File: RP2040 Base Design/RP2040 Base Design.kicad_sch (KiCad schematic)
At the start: 27 parts, among them J1 USB_B_Micro, J2 Conn_01x02, J3 RP2040_SWD, U1 RP2040, U2 AMS1117-3.3, U3 W25Q128JVS, Y1 X322512MSB4SI

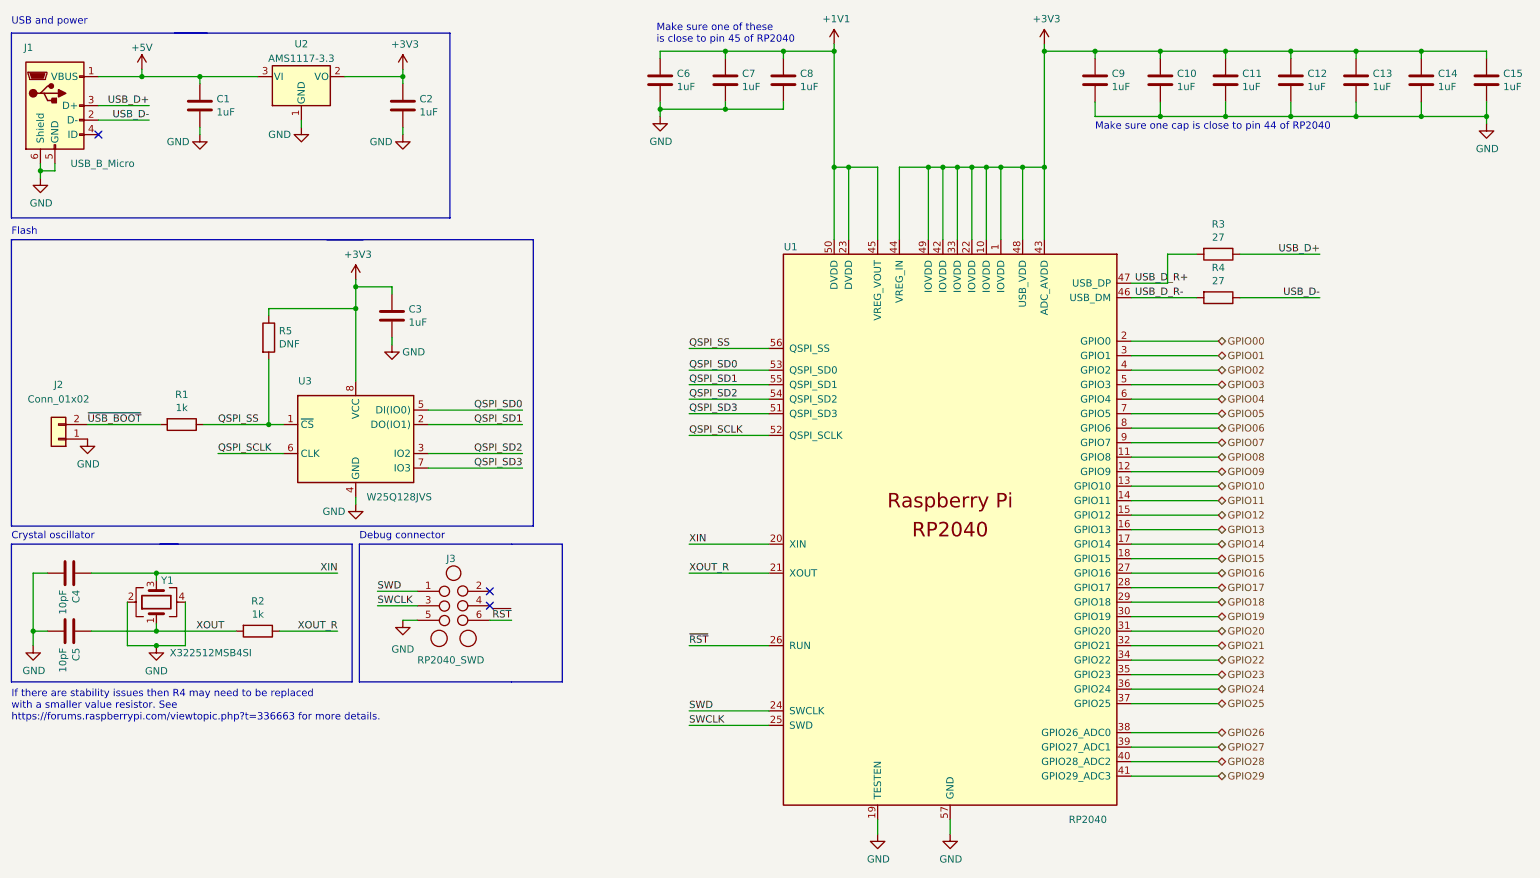
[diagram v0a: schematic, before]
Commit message: Move RP2040 to subsheet, fix up column names
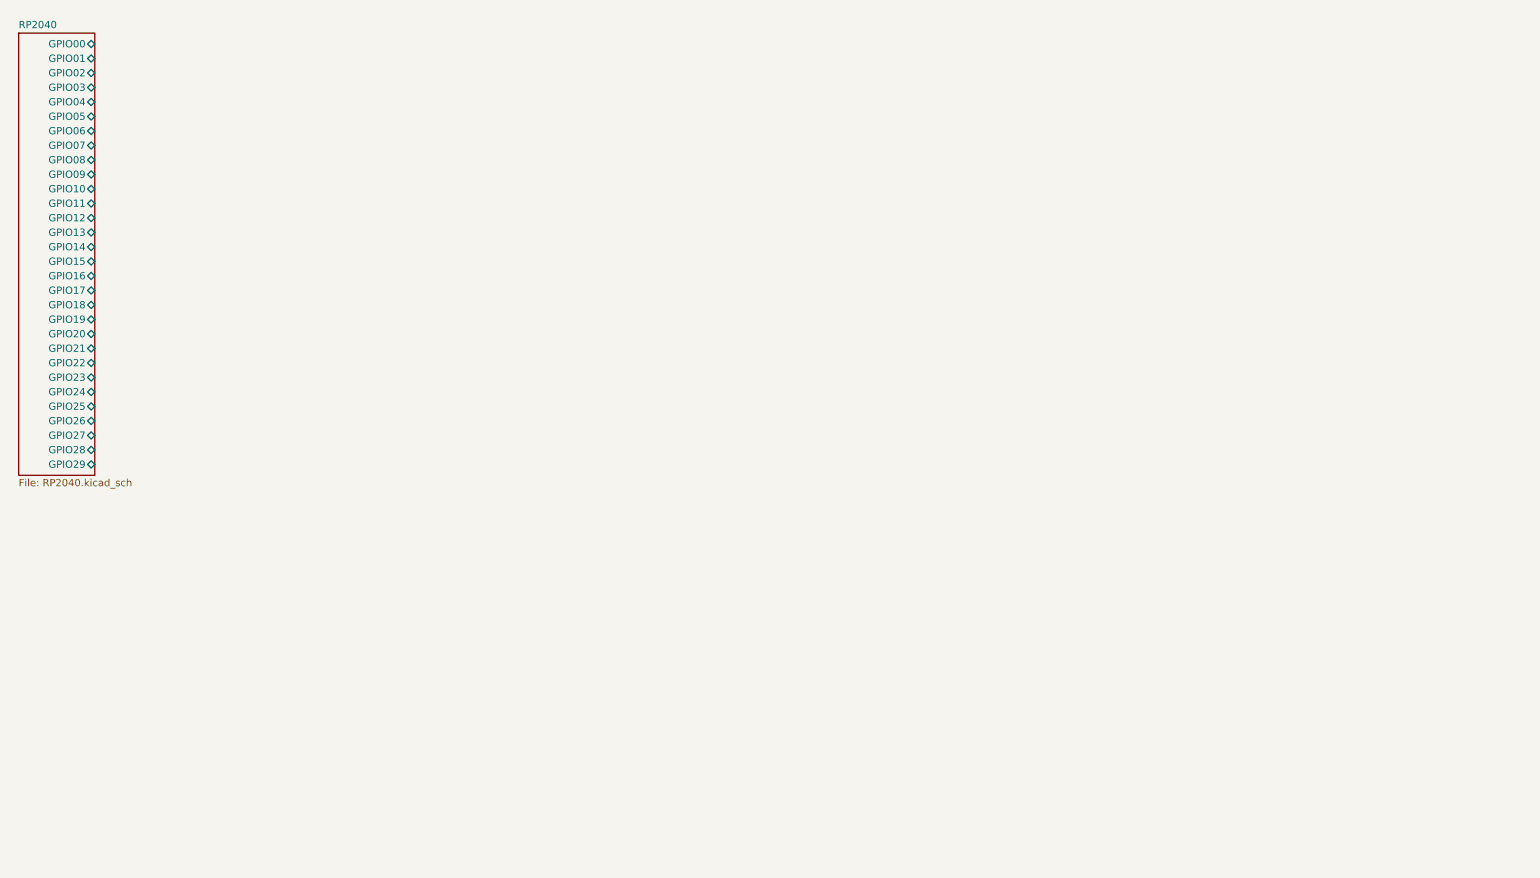
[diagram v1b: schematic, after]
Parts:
- removed C1, C10, C11, C12, C13, C14, C15, C2, C3, C6, C7, C8, C9: 1uF, Custom_Footprints:Perfect_0402, symbol Device:C
- removed C4, C5: 10pF, Custom_Footprints:Perfect_0402, symbol Device:C
- removed J1: USB_B_Micro, Custom_Footprints:USB_B_Mini_Amphenol_UE25BE5510H, symbol Connector:USB_B_Micro
- removed J2: Conn_01x02, Connector_PinHeader_2.54mm:PinHeader_1x02_P2.54mm_Vertical, symbol Connector_Generic:Conn_01x02
- removed J3: RP2040_SWD, Connector:Tag-Connect_TC2030-IDC-NL_2x03_P1.27mm_Vertical, symbol Custom_Symbols:TC2030-IDC-NL
- removed R1, R2: 1k, Custom_Footprints:Perfect_0402, symbol Device:R
- removed R3, R4: 27, Resistor_SMD:R_0603_1608Metric, symbol Device:R
- removed R5: DNF, Resistor_SMD:R_1206_3216Metric_Pad1.30x1.75mm_HandSolder, symbol Device:R
- removed U1: RP2040, Custom_Footprints:QFN56P40_700X700X90L40X18T310N, symbol Custom_Symbols:RP2040
- removed U2: AMS1117-3.3, Package_TO_SOT_SMD:SOT-223-3_TabPin2, symbol Regulator_Linear:AMS1117-3.3
- removed U3: W25Q128JVS, Package_SO:SOIC-8_5.23x5.23mm_P1.27mm, symbol Memory_Flash:W25Q128JVS
- removed Y1: X322512MSB4SI, Crystal:Crystal_SMD_3225-4Pin_3.2x2.5mm, symbol Device:Crystal_GND24
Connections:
- no-connect marks 3 -> 0
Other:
- added sheet RP2040 (RP2040.kicad_sch)
- note removed: "Crystal oscillator"
- note removed: "Debug connector"
- note removed: "Flash"
- note removed: "If there are stability issues then R4 may need to be replaced with a smaller value resistor. See https://forums.raspberrypi.com/viewtopic.php?t=336663 for more details."
- note removed: "Make sure one cap is close to pin 44 of RP2040"
- note removed: "Make sure one of these is close to pin 45 of RP2040"
- note removed: "USB and power"

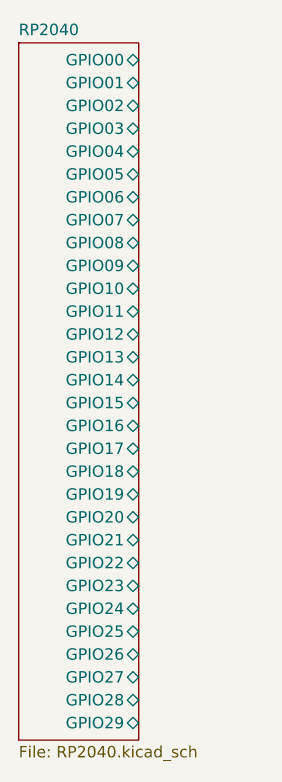
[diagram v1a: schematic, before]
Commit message: Add 10k pullup resistor to RUN pin for debugging Fixes #2
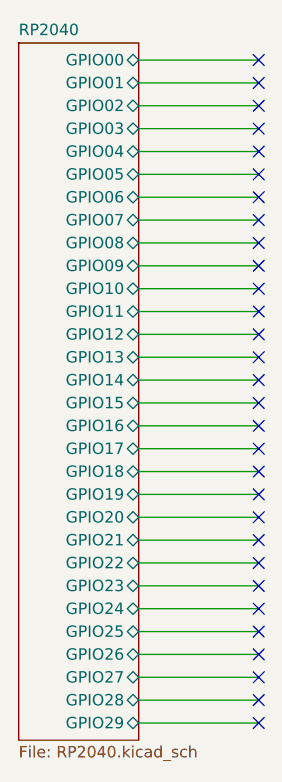
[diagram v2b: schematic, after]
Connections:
- no-connect marks 0 -> 30
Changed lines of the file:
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@@
     (rev "${VERSION}")
+  )
+  (no_connect (at 41.275 74.93))
+  (no_connect (at 41.275 31.75))
+  (no_connect (at 41.275 85.09))
+  (no_connect (at 41.275 46.99))
+  (no_connect (at 41.275 34.29))
+  (no_connect (at 41.275 39.37))
+  (no_connect (at 41.275 44.45))
+  (no_connect (at 41.275 57.15))
+  (no_connect (at 41.275 36.83))
+  (no_connect (at 41.275 54.61))
+  (no_connect (at 41.275 41.91))
+  (no_connect (at 41.275 87.63))
+  (no_connect (at 41.275 67.31))
+  (no_connect (at 41.275 52.07))
+  (no_connect (at 41.275 24.13))
+  (no_connect (at 41.275 82.55))
+  (no_connect (at 41.275 72.39))
+  (no_connect (at 41.275 19.05))
+  (no_connect (at 41.275 92.71))
+  (no_connect (at 41.275 59.69))
+  (no_connect (at 41.275 29.21))
+  (no_connect (at 41.275 77.47))
+  (no_connect (at 41.275 80.01))
+  (no_connect (at 41.275 64.77))
+  (no_connect (at 41.275 69.85))
+  (no_connect (at 41.275 21.59))
+  (no_connect (at 41.275 49.53))
+  (no_connect (at 41.275 62.23))
+  (no_connect (at 41.275 26.67))
+  (no_connect (at 41.275 90.17))
+  (wire (pts (xy 27.94 90.17) (xy 41.275 90.17))
+    (stroke (width 0) (type default) (color 0 0 0 0))
+  )
+  (wire (pts (xy 27.94 82.55) (xy 41.275 82.55))
+    (stroke (width 0) (type default) (color 0 0 0 0))
+  )
+  (wire (pts (xy 27.94 41.91) (xy 41.275 41.91))
+    (stroke (width 0) (type default) (color 0 0 0 0))
+  )
+  (wire (pts (xy 27.94 34.29) (xy 41.275 34.29))
+    (stroke (width 0) (type default) (color 0 0 0 0))
+  )
+  (wire (pts (xy 27.94 29.21) (xy 41.275 29.21))
+    (stroke (width 0) (type default) (color 0 0 0 0))
+  )
+  (wire (pts (xy 27.94 19.05) (xy 41.275 19.05))
+    (stroke (width 0) (type default) (color 0 0 0 0))
+  )
+  (wire (pts (xy 27.94 44.45) (xy 41.275 44.45))
+    (stroke (width 0) (type default) (color 0 0 0 0))
+  )
+  (wire (pts (xy 27.94 24.13) (xy 41.275 24.13))
+    (stroke (width 0) (type default) (color 0 0 0 0))
+  )
+  (wire (pts (xy 27.94 72.39) (xy 41.275 72.39))
+    (stroke (width 0) (type default) (color 0 0 0 0))
+  )
+  (wire (pts (xy 27.94 92.71) (xy 41.275 92.71))
+    (stroke (width 0) (type default) (color 0 0 0 0))
+  )
+  (wire (pts (xy 27.94 39.37) (xy 41.275 39.37))
+    (stroke (width 0) (type default) (color 0 0 0 0))
+  )
+  (wire (pts (xy 27.94 69.85) (xy 41.275 69.85))
+    (stroke (width 0) (type default) (color 0 0 0 0))
+  )
+  (wire (pts (xy 27.94 36.83) (xy 41.275 36.83))
+    (stroke (width 0) (type default) (color 0 0 0 0))
+  )
+  (wire (pts (xy 27.94 49.53) (xy 41.275 49.53))
+    (stroke (width 0) (type default) (color 0 0 0 0))
+  )
+  (wire (pts (xy 27.94 64.77) (xy 41.275 64.77))
+    (stroke (width 0) (type default) (color 0 0 0 0))
+  )
+  (wire (pts (xy 27.94 59.69) (xy 41.275 59.69))
+    (stroke (width 0) (type default) (color 0 0 0 0))
+  )
+  (wire (pts (xy 27.94 57.15) (xy 41.275 57.15))
+    (stroke (width 0) (type default) (color 0 0 0 0))
+  )
+  (wire (pts (xy 27.94 26.67) (xy 41.275 26.67))
+    (stroke (width 0) (type default) (color 0 0 0 0))
+  )
+  (wire (pts (xy 27.94 74.93) (xy 41.275 74.93))
+    (stroke (width 0) (type default) (color 0 0 0 0))
+  )
+  (wire (pts (xy 27.94 67.31) (xy 41.275 67.31))
+    (stroke (width 0) (type default) (color 0 0 0 0))
+  )
+  (wire (pts (xy 27.94 54.61) (xy 41.275 54.61))
+    (stroke (width 0) (type default) (color 0 0 0 0))
+  )
+  (wire (pts (xy 27.94 52.07) (xy 41.275 52.07))
+    (stroke (width 0) (type default) (color 0 0 0 0))
+  )
+  (wire (pts (xy 27.94 77.47) (xy 41.275 77.47))
+    (stroke (width 0) (type default) (color 0 0 0 0))
+  )
+  (wire (pts (xy 27.94 46.99) (xy 41.275 46.99))
+    (stroke (width 0) (type default) (color 0 0 0 0))
+  )
+  (wire (pts (xy 27.94 80.01) (xy 41.275 80.01))
+    (stroke (width 0) (type default) (color 0 0 0 0))
+  )
+  (wire (pts (xy 27.94 87.63) (xy 41.275 87.63))
+    (stroke (width 0) (type default) (color 0 0 0 0))
+  )
+  (wire (pts (xy 27.94 31.75) (xy 41.275 31.75))
+    (stroke (width 0) (type default) (color 0 0 0 0))
+  )
+  (wire (pts (xy 27.94 62.23) (xy 41.275 62.23))
+    (stroke (width 0) (type default) (color 0 0 0 0))
+  )
+  (wire (pts (xy 27.94 21.59) (xy 41.275 21.59))
+    (stroke (width 0) (type default) (color 0 0 0 0))
+  )
+  (wire (pts (xy 27.94 85.09) (xy 41.275 85.09))
+    (stroke (width 0) (type default) (color 0 0 0 0))
   )
   (sheet (at 14.605 17.145) (size 13.335 77.47) (fields_autoplaced)
@@
       (reference "#PWR01") (unit 1) (value "GND") (footprint "")
     )
+    (path "/99e5628a-8c61-4f9d-aa6e-5b585271b505/311b8624-7d9a-437a-9da5-5987fabc6fde"
+      (reference "#PWR02") (unit 1) (value "+3V3") (footprint "")
+    )
     (path "/99e5628a-8c61-4f9d-aa6e-5b585271b505/3f6a83ae-cff1-4c39-98be-8887d8ed4de6"
       (reference "#PWR05") (unit 1) (value "GND") (footprint "")
@@
       (reference "R5") (unit 1) (value "DNF") (footprint "Resistor_SMD:R_1206_3216Metric_Pad1.30x1.75mm_HandSolder")
     )
+    (path "/99e5628a-8c61-4f9d-aa6e-5b585271b505/7f2c9904-545b-4337-acd6-8707e0924818"
+      (reference "R6") (unit 1) (value "10k") (footprint "Custom_Footprints:Perfect_0402")
+    )
     (path "/99e5628a-8c61-4f9d-aa6e-5b585271b505/2262369d-908f-4b7b-8fa8-6f936456c0ae"
